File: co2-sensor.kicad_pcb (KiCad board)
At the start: 2 copper layers, 60 x 60 mm, 51 parts, among them J1 24-pin FPC Connector, J2 USB-C Receptacle, J3 JST 2-PH, Q1 AO3401A, Q2 AO3400A, SW1 SW_Push, SW2 SW_Push, SW3 SW_Push, SW4 SW_Push, SW5 SW_Push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

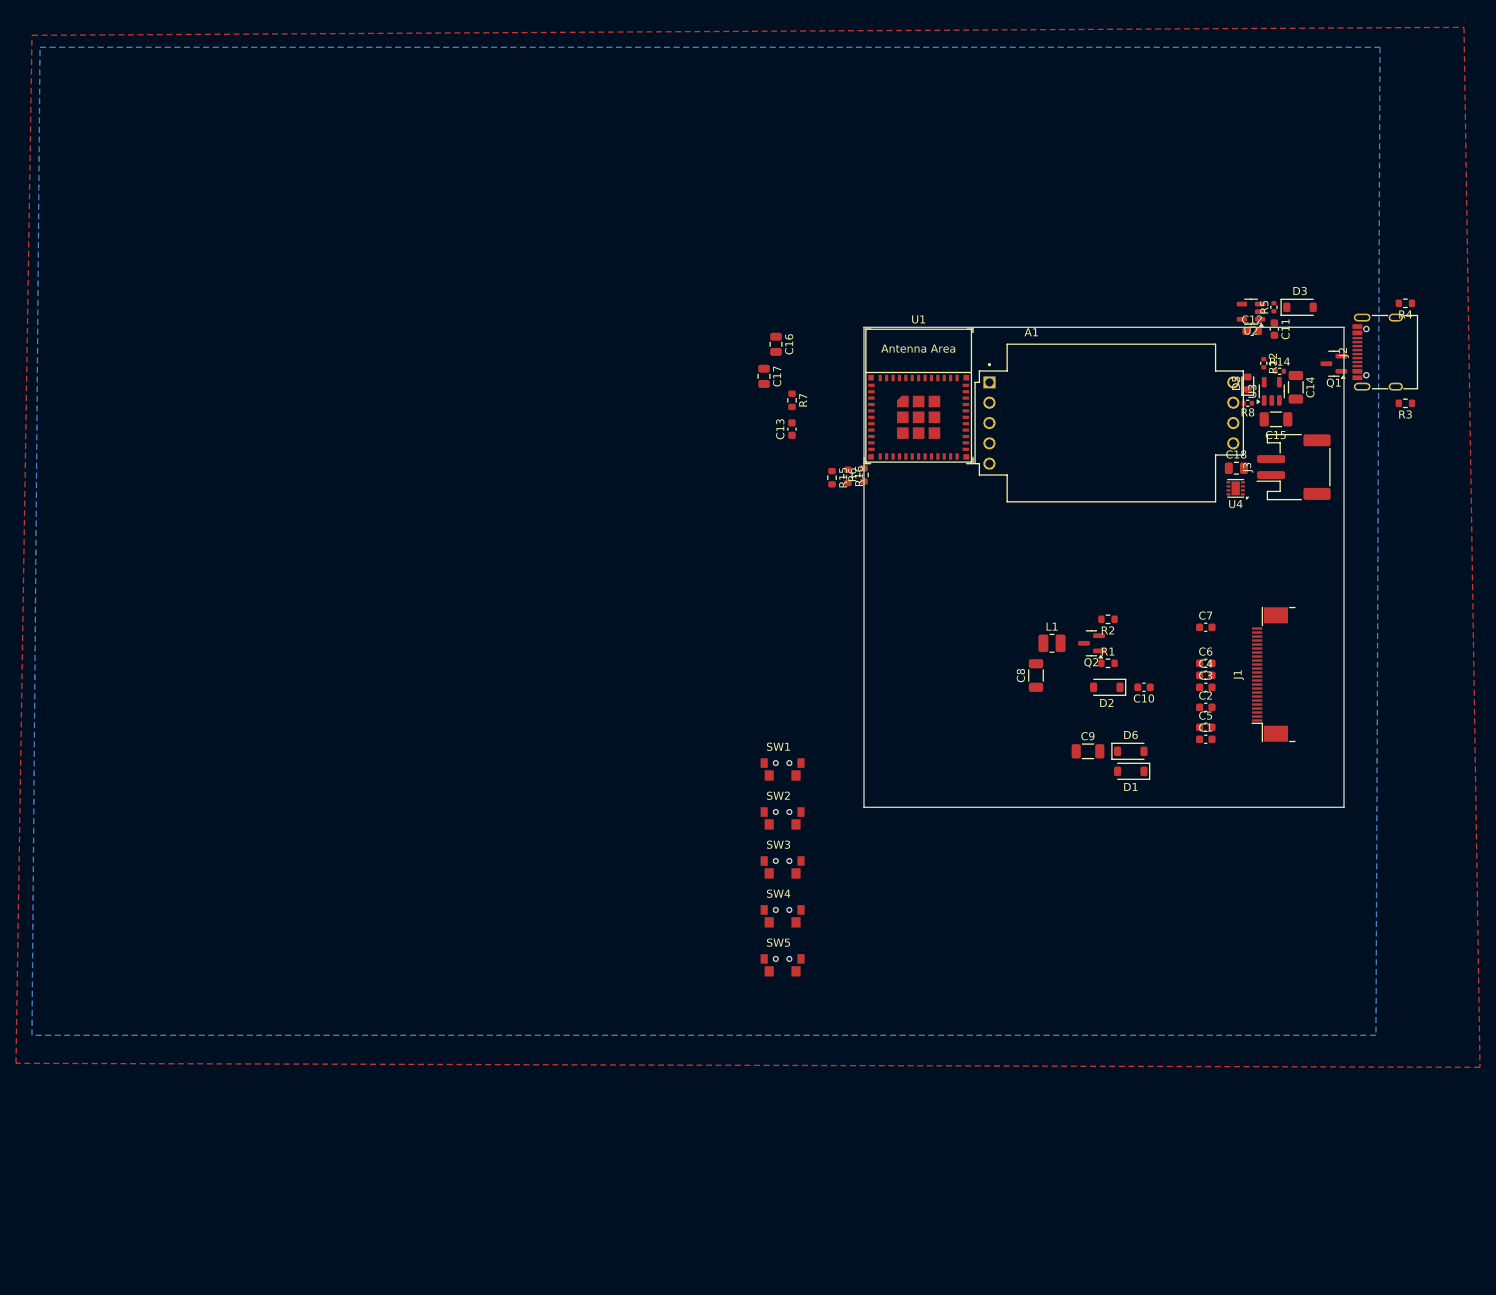
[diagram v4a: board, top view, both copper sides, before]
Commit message: Start connecting components for the e-ink display
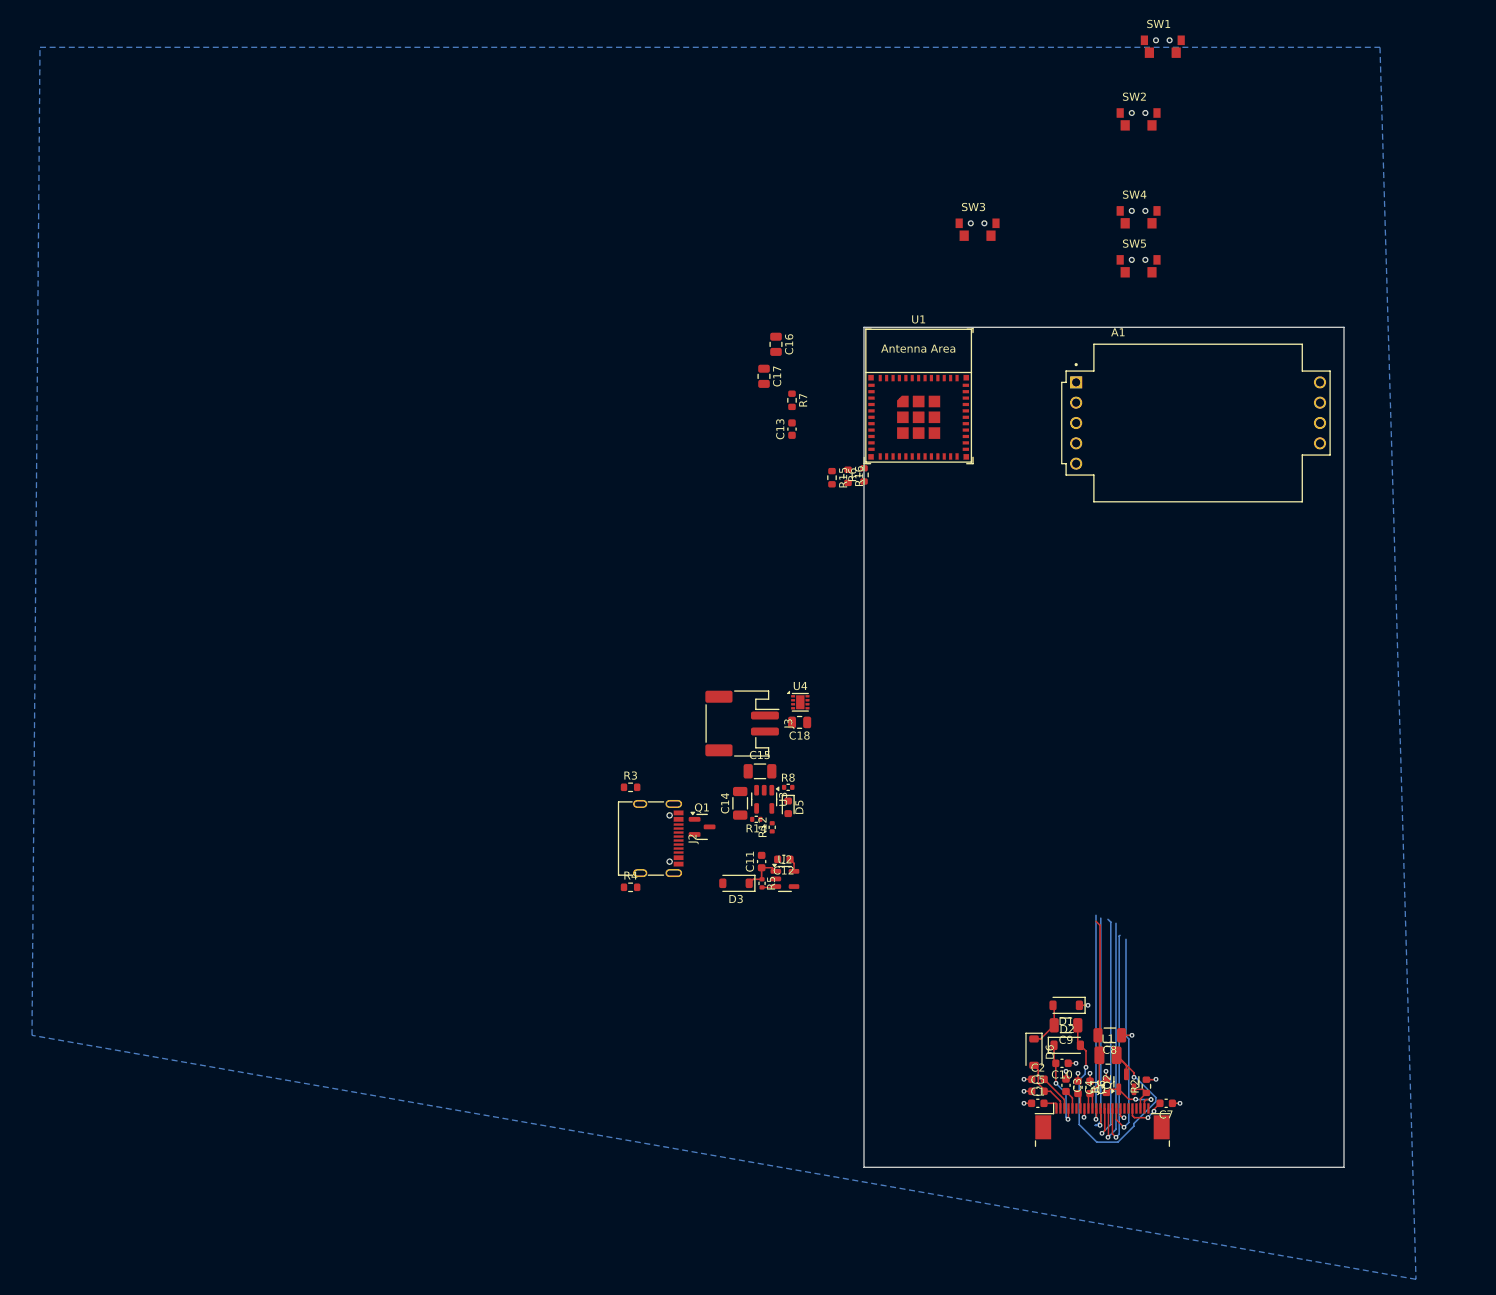
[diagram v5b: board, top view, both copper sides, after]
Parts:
- moved R4 121.3 mm to (101.8, 143.5), turned to 0 degrees
- moved J2 110.5 mm to (104.1, 137.4), turned to -90 degrees
- moved R3 108.1 mm to (101.8, 131.0), turned to 0 degrees
- moved SW1 102.1 mm to (168.3, 37.6)
- moved D3 100.8 mm to (115.0, 143.0), turned to 180 degrees
- moved SW2 98.1 mm to (165.3, 46.7)
- moved SW4 98.1 mm to (165.3, 59.0)
- moved SW5 98.1 mm to (165.3, 65.1)
- moved Q1 97.9 mm to (110.8, 135.9), turned to 0 degrees
- moved R5 96.3 mm to (118.3, 143.0), turned to -90 degrees
- moved C11 92.4 mm to (118.2, 140.3), turned to 90 degrees
- moved U2 91.8 mm to (121.1, 142.5), turned to 0 degrees
- moved C12 88.2 mm to (121.0, 140.0), turned to 180 degrees
- moved C14 86.8 mm to (115.5, 133.0), turned to 90 degrees
- moved R14 86.1 mm to (117.5, 135.0), turned to 180 degrees
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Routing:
- net Net-(D2-A): track 0.00 -> 36.8 mm, vias 0 -> 2
- net /EINK_DC: track 0.00 -> 31.1 mm, vias 0 -> 1
- net /EINK_CS: track 0.00 -> 30.6 mm, vias 0 -> 1
- net /EINK_RES: track 0.00 -> 29.2 mm, vias 0 -> 1
- net /EINK_SCLK: track 0.00 -> 29.1 mm, vias 0 -> 1
- net +3.3V: track 0.00 -> 28.0 mm
- net /EINK_MOSI: track 0.00 -> 26.9 mm, vias 0 -> 1
- net /EINK_BUSY: track 0.00 -> 26.6 mm, vias 0 -> 1
- net GND: track 0.00 -> 15.0 mm, vias 0 -> 14
- net /PREVGH: track 0.00 -> 11.4 mm, vias 0 -> 2
- net /GDR: track 0.00 -> 8.13 mm, vias 0 -> 2
- net /PREVGL: track 0.00 -> 7.22 mm
- net Net-(D1-A): track 0.00 -> 5.79 mm
- net Net-(J1-Pin_5): track 0.00 -> 5.36 mm, vias 0 -> 2
- net Net-(D3-K): track 0.00 -> 5.24 mm
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- removed copper zone on F.Cu, net GND
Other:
- board size 60 x 60 mm -> 60 x 105 mm

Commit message: Connect everything
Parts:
- SW1, SW2: footprint footprints:TS24CA -> Button_Switch_SMD:SW_Push_1P1T_XKB_TS-1187A
- SW3, SW4, SW5: footprint footprints:TS24CA -> footprints:SW-SMD_TS24CA
- moved SW1 63.6 mm to (135.9, 92.3), turned to 180 degrees
- moved J3 55.5 mm to (152.2, 81.1), turned to 0 degrees
- moved C1 53.4 mm to (153.4, 117.1)
- moved C10 53.4 mm to (156.4, 112.1)
- moved C2 53.4 mm to (153.4, 114.1)
- moved C3 53.4 mm to (156.9, 114.9)
- moved C4 53.4 mm to (158.4, 115.1)
- moved C5 53.4 mm to (153.4, 115.6)
- moved C6 53.4 mm to (159.9, 115.1)
- moved C7 53.4 mm to (169.5, 117.1)
- moved C8 53.4 mm to (162.4, 108.6)
- moved C9 53.4 mm to (156.9, 107.4)
- moved D1 53.4 mm to (157.0, 104.9)
- moved D2 53.4 mm to (157.1, 109.9)
- moved J1 53.4 mm to (161.5, 119.4)
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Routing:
- net +3.3V: track 28.0 -> 161.9 mm, vias 0 -> 6
- net GND: track 15.0 -> 89.4 mm, vias 14 -> 45
- net +BATT: track 0.00 -> 59.5 mm, vias 0 -> 2
- net /CO2_EN: track 0.00 -> 58.6 mm, vias 0 -> 1
- net /CO2_NRDY: track 0.00 -> 57.7 mm, vias 0 -> 1
- net /D-: track 0.00 -> 50.0 mm, vias 0 -> 4
- net /D+: track 0.00 -> 49.5 mm, vias 0 -> 6
- net /BTN3: track 0.00 -> 44.8 mm, vias 0 -> 4
- net /I2C_SCL: track 0.00 -> 42.3 mm, vias 0 -> 8
- net /I2C_SDA: track 0.00 -> 40.3 mm, vias 0 -> 8
- net /BTN2: track 0.00 -> 37.0 mm, vias 0 -> 4
- net /EINK_BUSY: track 26.6 -> 57.5 mm, vias 1 -> 2
- net /BTN1: track 0.00 -> 27.1 mm, vias 0 -> 2
- net VBUS: track 0.00 -> 26.4 mm, vias 0 -> 2
- net Net-(D2-A): track 36.8 -> 11.5 mm
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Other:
- board size 60 x 105 mm -> 61 x 61 mm

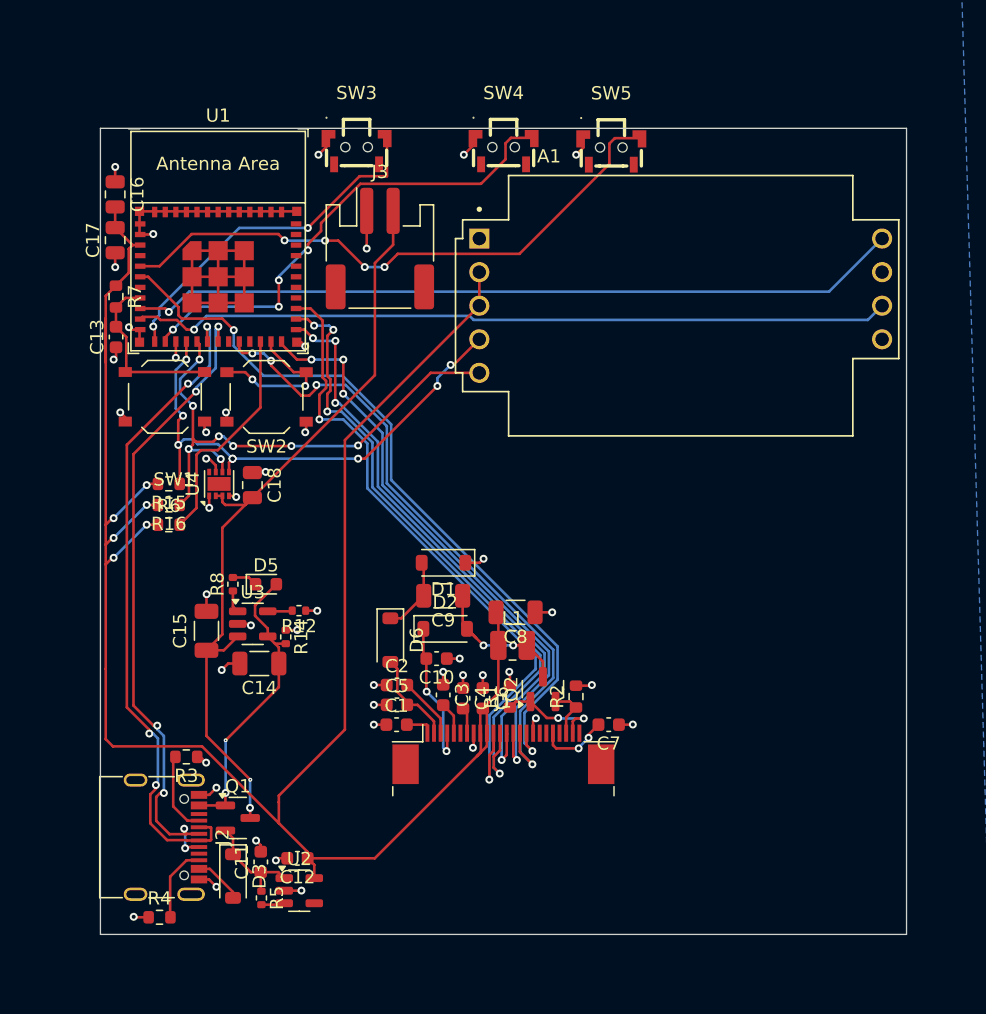
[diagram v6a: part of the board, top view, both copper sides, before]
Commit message: Apply some DRC tips
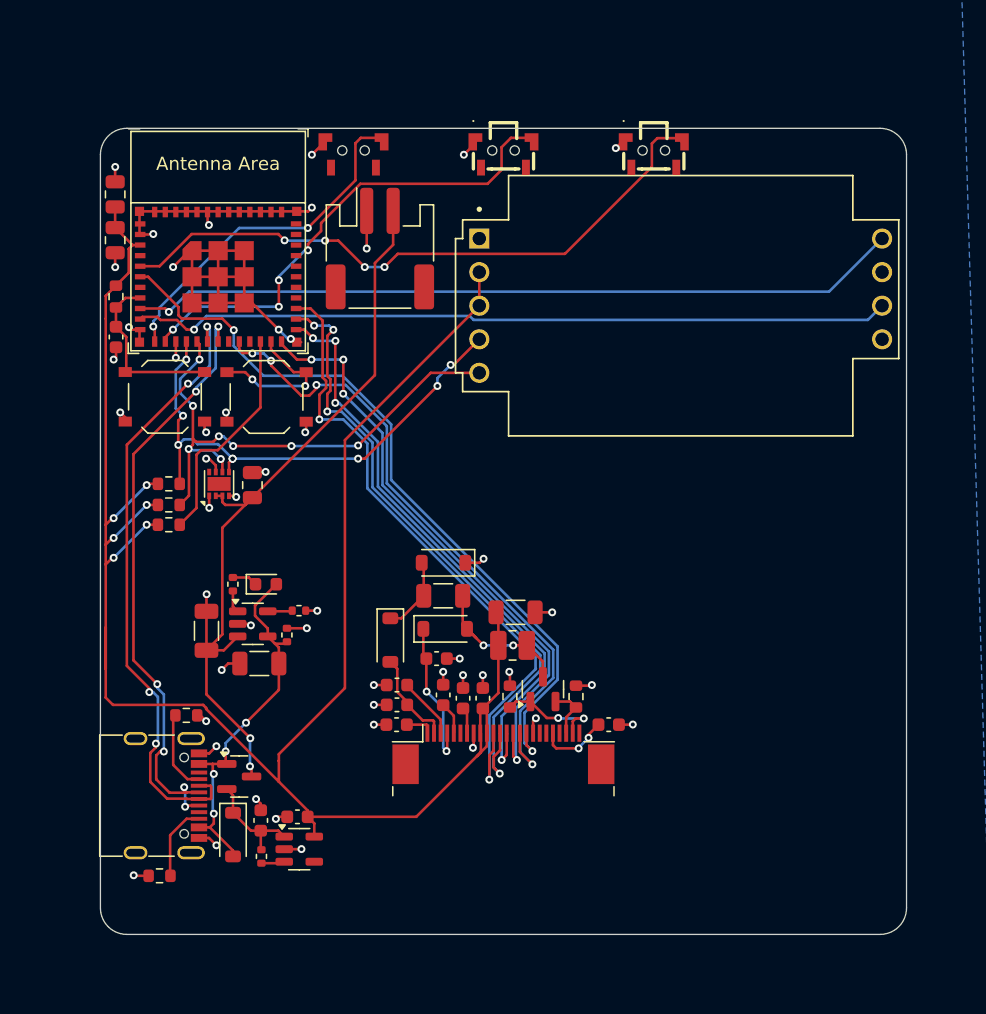
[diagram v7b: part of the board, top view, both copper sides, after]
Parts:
- moved SW5 3.22 mm to (172.9, 74.0)
- moved Q1 3.14 mm to (141.5, 121.0)
- moved U2 3.14 mm to (146.0, 126.5)
- moved C11 3.14 mm to (143.1, 124.4)
- moved C12 3.14 mm to (145.9, 124.1)
- moved D3 3.14 mm to (141.0, 125.4)
- moved J2 3.14 mm to (134.7, 122.5)
- moved R3 3.14 mm to (137.5, 116.4)
- moved R4 3.14 mm to (135.5, 128.6)
- moved R5 3.14 mm to (143.2, 127.1)
- moved SW3 0.34 mm to (150.2, 74.0)
- moved SW4 0.25 mm to (161.5, 74.0)
- moved R14 0.17 mm to (145.1, 110.3)
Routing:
- net GND: track 89.4 -> 98.5 mm, vias 45 -> 49
- net +3.3V: track 161.9 -> 154.1 mm
- net /BTN3: track 44.8 -> 48.2 mm
- net /D+: track 49.5 -> 46.2 mm
- net /D-: track 50.0 -> 46.9 mm
- net VBUS: track 26.4 -> 28.5 mm, vias 2 -> 4
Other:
- outline, holes or cut-outs redrawn
